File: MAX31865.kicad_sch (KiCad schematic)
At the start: 35 parts, among them J1 RTDSensor, J3 Conn_01x08, U1 MAX31865, U2 MIC5225, U3 74LVC125

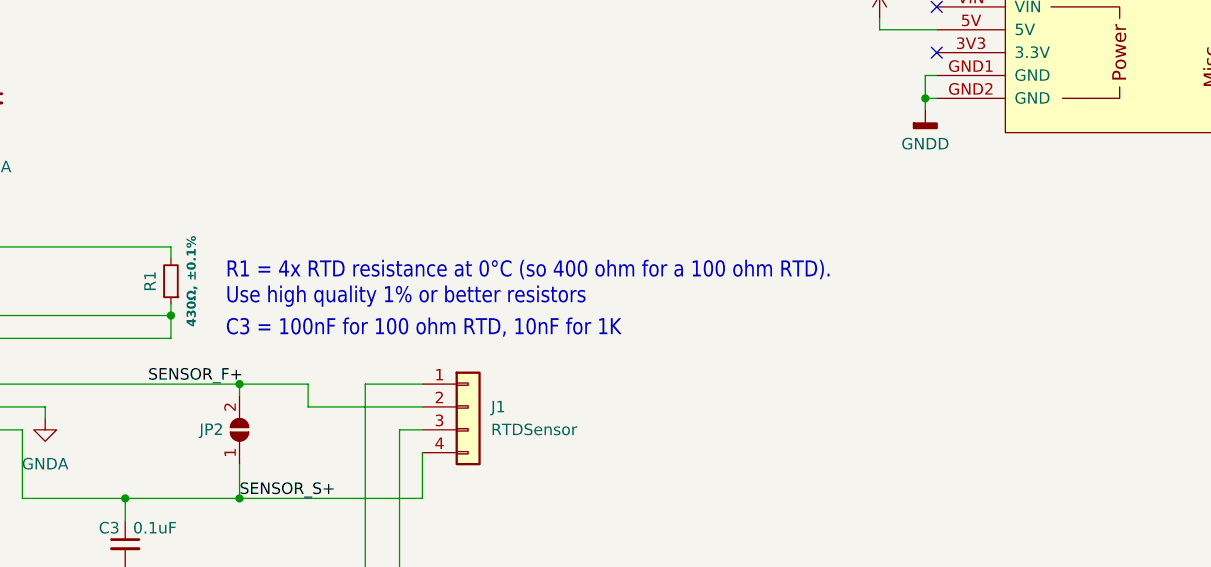
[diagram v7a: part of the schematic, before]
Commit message: fabrication outputs layout pdf
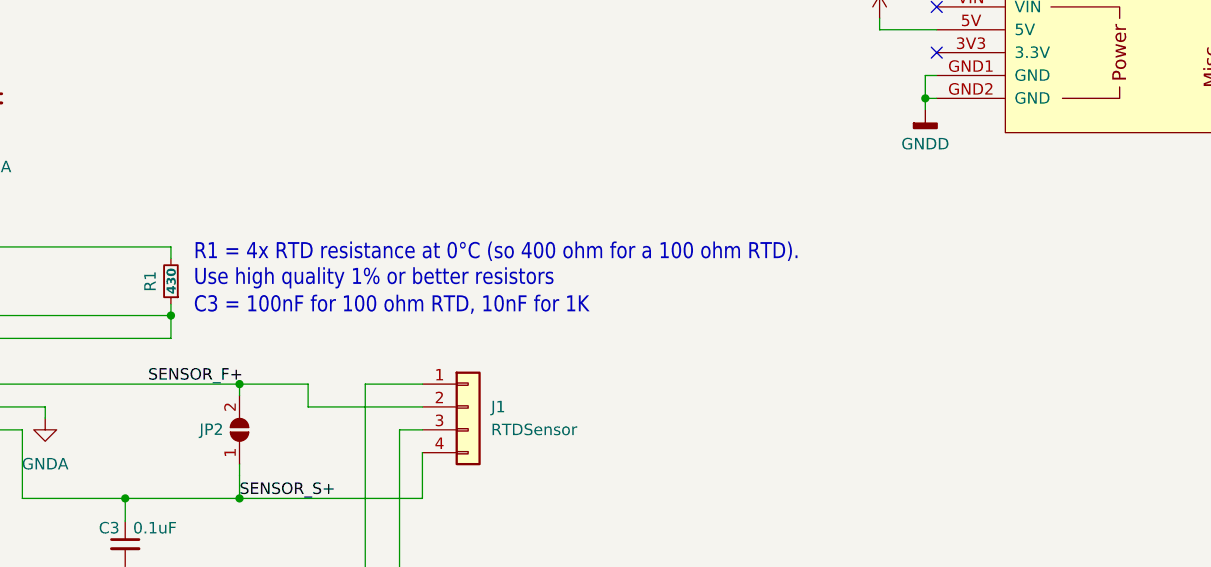
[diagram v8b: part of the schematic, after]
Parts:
- R1: value 430Ω, ±0.1% -> 430; Tolerance (none) -> Plus-Minus 0.1%
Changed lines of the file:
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@@
 	(text "R1 = 4x RTD resistance at 0°C (so 400 ohm for a 100 ohm RTD).\nUse high quality 1% or better resistors"
 		(exclude_from_sim no)
-		(at 136.906 137.414 0)
+		(at 133.35 135.382 0)
 		(effects
 			(font
@@
 	(text "C3 = 100nF for 100 ohm RTD, 10nF for 1K"
 		(exclude_from_sim no)
-		(at 136.906 140.97 0)
+		(at 133.35 138.43 0)
 		(effects
 			(font
@@
 			)
 		)
-		(property "Value" "430Ω, ±0.1%"
-			(at 133.096 134.62 90)
+		(property "Value" "430"
+			(at 130.8675 134.6008 90)
 			(effects
 				(font
@@
 			(effects
 				(font
+					(size 1.27 1.27)
+				)
+				(hide yes)
+			)
+		)
+		(property "Tolerance" "Plus-Minus 0.1%"
+			(at 130.81 134.62 90)
+			(effects
+				(font
